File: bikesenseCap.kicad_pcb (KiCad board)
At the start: 2 copper layers, 66 x 66 mm, 58 parts, among them J1 I2C Connector, J10 Wake, J11 RST, J2 PAD, J3 PAD, J4 PAD, J5 PAD, U1 CCS811, U2 cap1188, U3 TCA9534

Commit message: up to revB
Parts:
- added G***: LOGO, graphics:Negative Sized, B.Cu at (142.0, 81.0)
- added REF**: MountingHole_3mm, Mounting_Holes:MountingHole_3mm, F.Cu at (141.0, 94.0)
- added REF**: MountingHole_3mm, Mounting_Holes:MountingHole_3mm, F.Cu at (141.0, 105.0)
- D11, D12, D13, D14, D15, D16, D17, D18: footprint LEDs:LED_0805_HandSoldering -> revLed:LED_1206_3216Metric_ReverseMount_Hole1.8x2.4mm
- J1: value I2C Connector -> Conn_01x04_Male
- J10: value Wake -> Conn_01x01
- J11: value RST -> Conn_01x01
- moved R6 2.15 mm to (145.0, 107.9)
- moved D17 1.42 mm to (171.0, 121.0), turned to 225 degrees
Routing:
- net /SDA: track 137.6 -> 124.8 mm
- net +3V3: track 359.0 -> 369.3 mm, vias 0 -> 2
- net Net-(D6-Pad1): track 50.0 -> 44.7 mm
- net /SouthEast: track 25.7 -> 20.8 mm
- net Net-(D17-Pad2): track 11.4 -> 6.94 mm
- net /SCL: track 132.7 -> 136.0 mm
- net Net-(D12-Pad2): track 10.8 -> 12.4 mm
- net /West: track 52.4 -> 53.8 mm
- net /North: track 61.5 -> 60.0 mm, vias 0 -> 2
- net /NorthWest: track 85.4 -> 86.3 mm
- net Net-(TH1-Pad1): track 41.1 -> 40.4 mm
- net Net-(D13-Pad2): track 7.81 -> 8.40 mm
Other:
- board text added: "REV B"
- board text removed: "REV A"

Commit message: REV C
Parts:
- removed D1, D2: 1N4148, Diodes_SMD:D_SOD-123
- removed G***: LOGO, graphics:Negative Sized
- removed J10, J11: Conn_01x01, Connectors:1X01
- removed JP1: SolderJumper_2_Bridged, Jumpers:SMT-JUMPER_2_NO_SILK
- removed REF** (x2): MountingHole_3mm, Mounting_Holes:MountingHole_3mm
- R9: value 100K -> 10K
- moved TH1 10.2 mm to (132.1, 117.9), turned to 90 degrees
- moved R12 4.40 mm to (152.2, 88.9)
- moved R7 4.31 mm to (129.5, 109.0)
- moved R4 2.34 mm to (133.3, 83.7)
- moved R6 2.20 mm to (145.0, 110.1), turned to 270 degrees
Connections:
- R7 pad 1: Net-(R7-Pad1) -> +3V3
- R9 pad 1: Net-(D1-Pad2) -> Net-(R9-Pad1)
- TH1 pad 1: Net-(TH1-Pad1) -> Net-(R9-Pad1)
- TH1 pad 2: +3V3 -> Net-(TH1-Pad2)
- U1 pad 1: Net-(R7-Pad1) -> GND
- U1 pad 4: Net-(TH1-Pad1) -> Net-(TH1-Pad2)
- U1 pad 5: Net-(TH1-Pad1) -> Net-(TH1-Pad2)
- U1 pad 7: Net-(D1-Pad2) -> GND
- U1 pad 8: +3V3 -> Net-(R9-Pad1)
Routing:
- net +3V3: track 369.3 -> 326.4 mm, vias 2 -> 4
- net Net-(TH1-Pad1): track 40.4 -> 0.00 mm
- net Net-(R9-Pad1): track 0.00 -> 25.7 mm, vias 0 -> 2
- net Net-(D1-Pad2): track 15.6 -> 0.00 mm
- net Net-(D1-Pad1): track 15.5 -> 0.00 mm, vias 1 -> 0
- net Net-(R10-Pad1): track 18.9 -> 6.44 mm
- net Net-(TH1-Pad2): track 0.00 -> 9.32 mm
- net Net-(R7-Pad1): track 6.28 -> 0.00 mm
- net /SouthWest: track 47.4 -> 52.2 mm
- net GND: track 143.2 -> 148.0 mm
- net Net-(D3-Pad1): track 17.8 -> 22.2 mm
- net Net-(D4-Pad2): track 6.38 -> 2.13 mm, vias 2 -> 0
- net Net-(D2-Pad1): track 4.11 -> 0.00 mm
- net /SDA: track 124.8 -> 122.3 mm
- net /SCL: track 136.0 -> 138.1 mm
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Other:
- board text added: "1"
- board text added: "E"
- board text added: "N"
- board text added: "REV C"
- board text added: "S"
- board text added: "W"
- board text removed: "REV B"

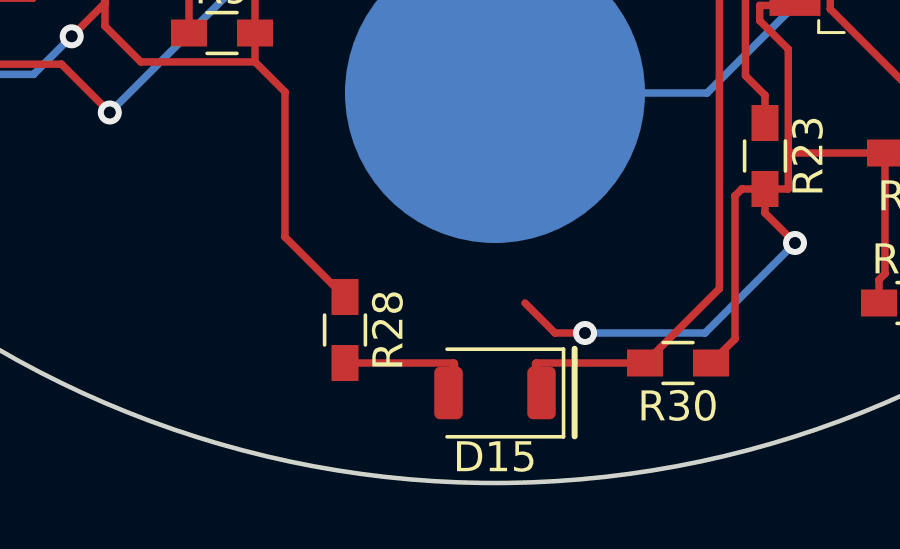
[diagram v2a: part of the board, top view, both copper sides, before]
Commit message: Added MISSING trace
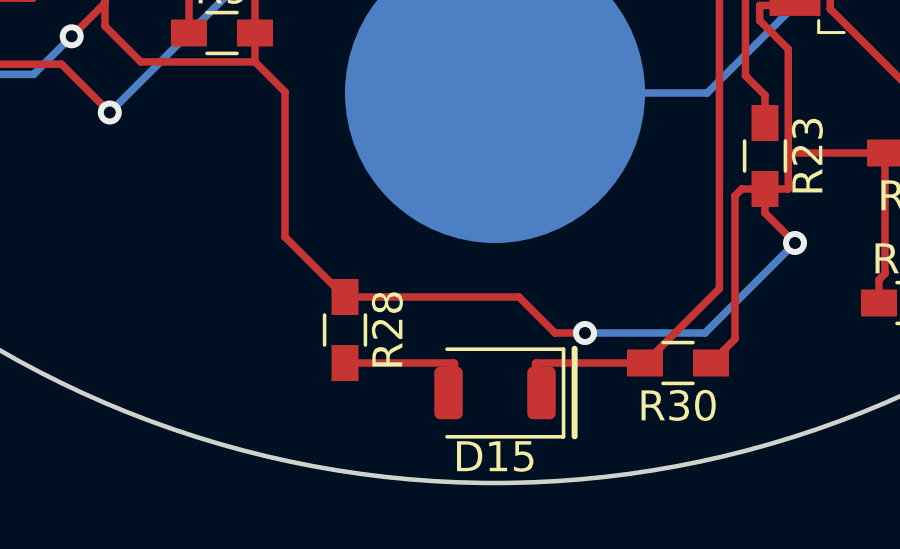
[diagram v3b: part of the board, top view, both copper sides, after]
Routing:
- net +3V3: track 326.4 -> 332.5 mm
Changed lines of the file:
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@@
     (thickness 1.6)
     (drawings 21)
-    (tracks 587)
+    (tracks 588)
     (zones 0)
     (modules 53)
@@
   (title_block
     (title Bikesense)
-    (date 2019-01-02)
-    (rev "REV B")
+    (date 2019-03-04)
+    (rev "REV D")
     (company "David Dressner")
   )
@@
   (segment (start 122.85 98.863589) (end 122.1 98.113589) (width 0.25) (layer F.Cu) (net 27))
   (via (at 160 125) (size 0.8) (drill 0.4) (layers F.Cu B.Cu) (net 27))
-  (segment (start 152 128) (end 151 127) (width 0.25) (layer F.Cu) (net 27))
-  (segment (start 153 128) (end 152 128) (width 0.25) (layer F.Cu) (net 27))
   (segment (start 157 128) (end 153 128) (width 0.25) (layer B.Cu) (net 27))
   (segment (start 160 125) (end 157 128) (width 0.25) (layer B.Cu) (net 27))
@@
   (segment (start 157.930011 89.350011) (end 154.94 86.36) (width 0.25) (layer F.Cu) (net 27))
   (segment (start 157.930011 103.0064) (end 157.930011 89.350011) (width 0.25) (layer F.Cu) (net 27))
+  (segment (start 150.8 126.8) (end 145 126.8) (width 0.25) (layer F.Cu) (net 27))
+  (segment (start 153 128) (end 152 128) (width 0.25) (layer F.Cu) (net 27))
+  (segment (start 152 128) (end 150.8 126.8) (width 0.25) (layer F.Cu) (net 27))
   (segment (start 168.4986 115.81) (end 168.2047 115.81) (width 0.25) (layer F.Cu) (net 28))
   (segment (start 168.7924 115.81) (end 168.4986 115.81) (width 0.25) (layer F.Cu) (net 28) (status 10))

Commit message: update
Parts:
- removed R10: 100K, Resistors_SMD:R_0603_HandSoldering
- removed TH1: 10K ntc, Resistors_SMD:R_0603_HandSoldering
- added AE1: W3011, antenna:w3011, F.Cu at (140.5, 128.0)
- added G***: LOGO, graphics:Negative Sized, B.Cu at (140.0, 85.0)
- added J6: ufl, .pretty:ufl, F.Cu at (134.5, 124.0)
- R19, R21, R22, R27, R28, R31, R32, R35: value 66 -> 100
- R7: value 100K -> 10K
- U1: value CCS811 -> bme680; footprint digikey-footprints:VOC_Sensor_LGA-10-1EP-2.7x4mm_CCS811B -> kicad-libraries:BME680
- moved U1 4.72 mm to (134.4, 113.9), turned to 270 degrees
- moved R22 4.10 mm to (129.0, 117.1), turned to 90 degrees
- moved R31 2.19 mm to (165.0, 75.9), turned to 90 degrees
- moved R32 1.86 mm to (165.0, 125.5), turned to 270 degrees
- moved R35 1.56 mm to (179.2, 91.9), turned to 270 degrees
- moved R27 1.41 mm to (155.0, 72.0), turned to 270 degrees
- moved R19 1.10 mm to (121.0, 106.1), turned to 90 degrees
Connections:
- R7 pad 1: +3V3 -> /SDA
- R7 pad 2: GND -> +3V3
- R8 pad 1: /SDA -> Net-(R8-Pad1)
- U1 pad 2: Net-(R10-Pad1) -> Net-(R8-Pad1)
- U1 pad 3: Net-(U1-Pad3) -> /SDA
- U1 pad 4: Net-(TH1-Pad2) -> /SCL
- U1 pad 5: Net-(TH1-Pad2) -> Net-(R9-Pad1)
- U1 pad 8: Net-(R9-Pad1) -> +3V3
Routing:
- net +3V3: track 332.5 -> 350.4 mm
- net Net-(R9-Pad1): track 25.7 -> 8.08 mm, vias 2 -> 0
- net /SDA: track 122.3 -> 139.5 mm, vias 2 -> 4
- net GND: track 148.0 -> 137.6 mm
- net Net-(TH1-Pad2): track 9.32 -> 0.00 mm
- net GNDS: track 0.00 -> 8.87 mm
- net Net-(AE1-Pad1): track 0.00 -> 7.99 mm
- net Net-(R8-Pad1): track 0.00 -> 7.91 mm
- net Net-(R10-Pad1): track 6.44 -> 0.00 mm
- net Net-(J5-Pad1): track 53.9 -> 57.0 mm
- net Net-(D14-Pad2): track 6.88 -> 9.94 mm
- net Net-(J4-Pad1): track 36.9 -> 39.8 mm
- net Net-(J3-Pad1): track 29.8 -> 32.1 mm
- net /NorthWest: track 86.0 -> 84.6 mm
- net Net-(D3-Pad1): track 22.2 -> 21.3 mm
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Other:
- board text added: "PROD A"
- board text removed: "REV C"

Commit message: Removed GPS and CAPsenseing led from broad
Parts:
- removed AE1: W3011, antenna:w3011
- removed D3, D4, D5, D6: LED_Small, LEDs:LED_0603_HandSoldering
- removed J6: ufl, .pretty:ufl
- removed R11, R12, R13, R14: 470, Resistors_SMD:R_0603_HandSoldering
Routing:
- net Net-(U2-Pad8): track 46.3 -> 0.00 mm
- net Net-(U2-Pad7): track 35.1 -> 0.00 mm, vias 2 -> 0
- net +3V3: track 350.4 -> 317.7 mm
- net Net-(U2-Pad5): track 21.3 -> 0.00 mm, vias 2 -> 0
- net Net-(U2-Pad6): track 13.4 -> 0.00 mm
- net GNDS: track 8.87 -> 0.00 mm
- net Net-(AE1-Pad1): track 7.99 -> 0.00 mm
- net Net-(D5-Pad2): track 5.75 -> 0.00 mm
- net Net-(D6-Pad2): track 5.37 -> 0.00 mm
- net Net-(D3-Pad2): track 2.80 -> 0.00 mm
- net Net-(D4-Pad2): track 2.13 -> 0.00 mm
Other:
- board text added: "PROD B"
- board text removed: "PROD A"
